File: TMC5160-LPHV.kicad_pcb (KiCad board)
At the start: 2 copper layers, 15.5 x 20.3 mm, 8 parts, among them J1 StepStick Left, J2 StepStick Right, J3 StepStick Diag, Q1 DMT6018LDR, Q2 DMT6018LDR, Q3 DMT6018LDR, Q4 DMT6018LDR, U1 TMC5160A-TA

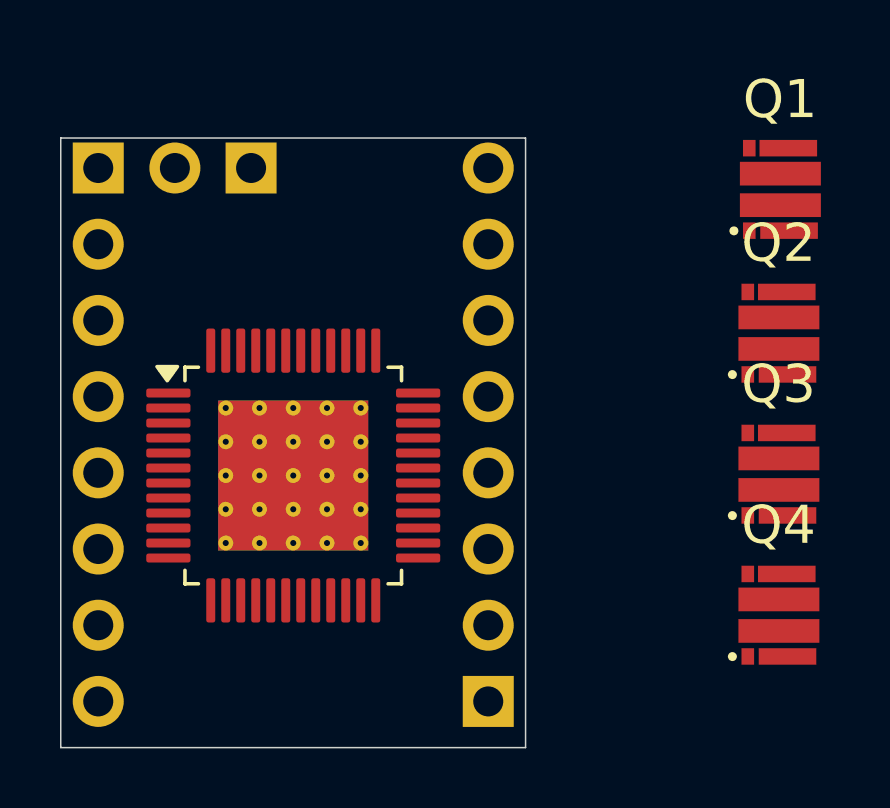
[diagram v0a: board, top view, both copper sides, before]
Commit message: switch to four-layer, minor improvements
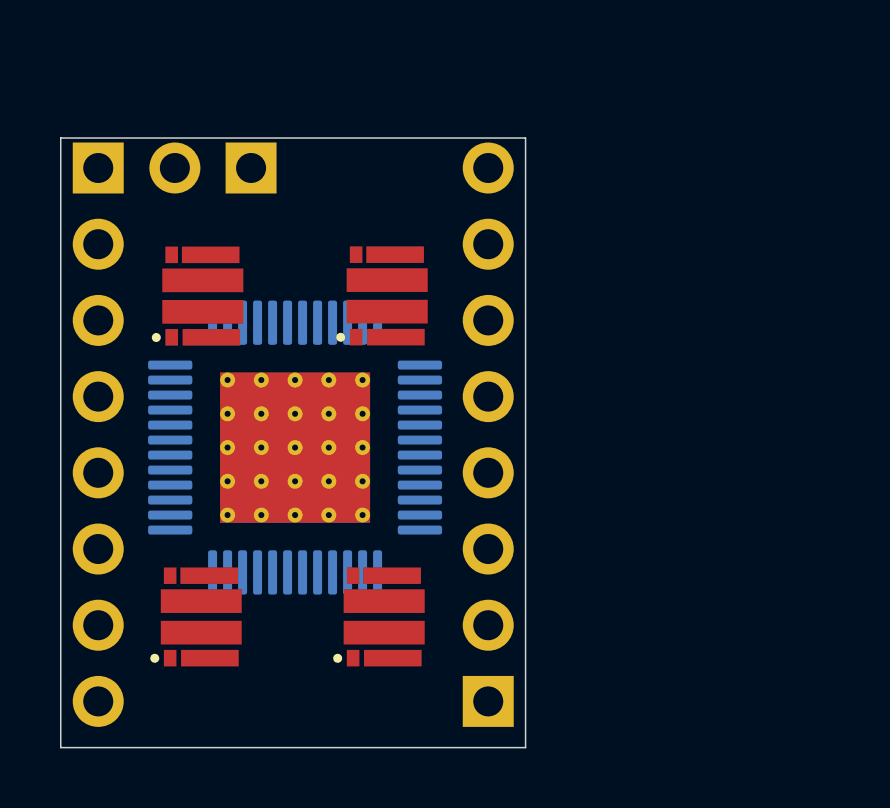
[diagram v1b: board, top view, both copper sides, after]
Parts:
- U1: moved to B.Cu
- moved Q3 19.8 mm to (137.7, 65.7)
- moved Q1 19.6 mm to (137.7, 55.0)
- moved Q4 13.2 mm to (143.8, 65.7)
- moved Q2 13.1 mm to (143.9, 55.0)
- moved U1 0.93 mm to (140.8, 60.1), turned to -90 degrees
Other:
- copper layers 2 -> 4
